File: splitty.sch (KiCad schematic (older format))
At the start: 97 parts, among them J1 USB_B_Micro, J2 USB_B_Micro, J3 Conn_01x06, J4 Conn_01x05, SW0 SW_Push, SW1 SW_Push, SW10 SW_Push, SW11 SW_Push, SW12 SW_Push, SW13 SW_Push, SW14 SW_Push, SW16 SW_Push, SW17 SW_Push, SW18 SW_Push, SW19 SW_Push, SW2 SW_Push, SW20 SW_Push, SW21 SW_Push, SW24 SW_Push, SW25 SW_Push, SW26 SW_Push, SW27 SW_Push, SW28 SW_Push, SW29 SW_Push, SW3 SW_Push, SW30 SW_Push, SW34 SW_Push, SW35 SW_Push, SW36 SW_Push, SW37 SW_Push, SW38 SW_Push, SW4 SW_Push, SW40 SW_Push, SW5 SW_Push, SW6 SW_Push, SW8 SW_Push, SW9 SW_Push, U1 ATmega32U4-AU, U2 USBLC6-2, U3 USBLC6-2, Y1 16M

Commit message: Update to Kicad 5
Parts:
- C1, C10, C11, C12, C3, C4, C5, C6, C7, C8, C9: footprint Capacitor_SMD:C_0603_1608Metric_Pad0.84x1.00mm_HandSolder -> Capacitor_SMD:C_0603_1608Metric_Pad1.05x0.95mm_HandSolder; symbol C -> Device:C
- D0, D1, D10, D11, D12, D13, D14, D16, D17, D18, D19, D2, D20, D21, D24, D25, D26, D27, D28, D29, D3, D30, D34, D35, D36, D37, D38, D4, D5, D6, D8, D9: symbol D -> Device:D
- J1, J2: symbol USB_B_Micro -> Connector:USB_B_Micro
- J3: symbol Conn_01x06 -> Connector_Generic:Conn_01x06
- J4: symbol Conn_01x05 -> Connector_Generic:Conn_01x05
- MK1, MK2, MK3, MK4, MK5, MK6, MK7, MK8: symbol Mounting_Hole -> Mechanical:MountingHole
- R1, R2, R3, R4, R5: footprint Resistor_SMD:R_0603_1608Metric_Pad0.84x1.00mm_HandSolder -> Resistor_SMD:R_0603_1608Metric_Pad1.05x0.95mm_HandSolder; symbol R -> Device:R
- SW0, SW1, SW10, SW11, SW12, SW13, SW14, SW16, SW17, SW18, SW19, SW2, SW20, SW21, SW24, SW25, SW26, SW27, SW28, SW29, SW3, SW30, SW34, SW35, SW36, SW37, SW38, SW4, SW40, SW5, SW6, SW8, SW9: symbol SW_Push -> Switch:SW_Push
- U1: symbol ATmega32U4-AU -> MCU_Microchip_ATmega:ATmega32U4-AU
- U2, U3: symbol USBLC6-2 -> splitty:USBLC6-2
- Y1: symbol Crystal -> Device:Crystal
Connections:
- wire segments 151 -> 219
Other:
- moved on the sheet: C1, C3, C4, C5, R3, SW40, Y1

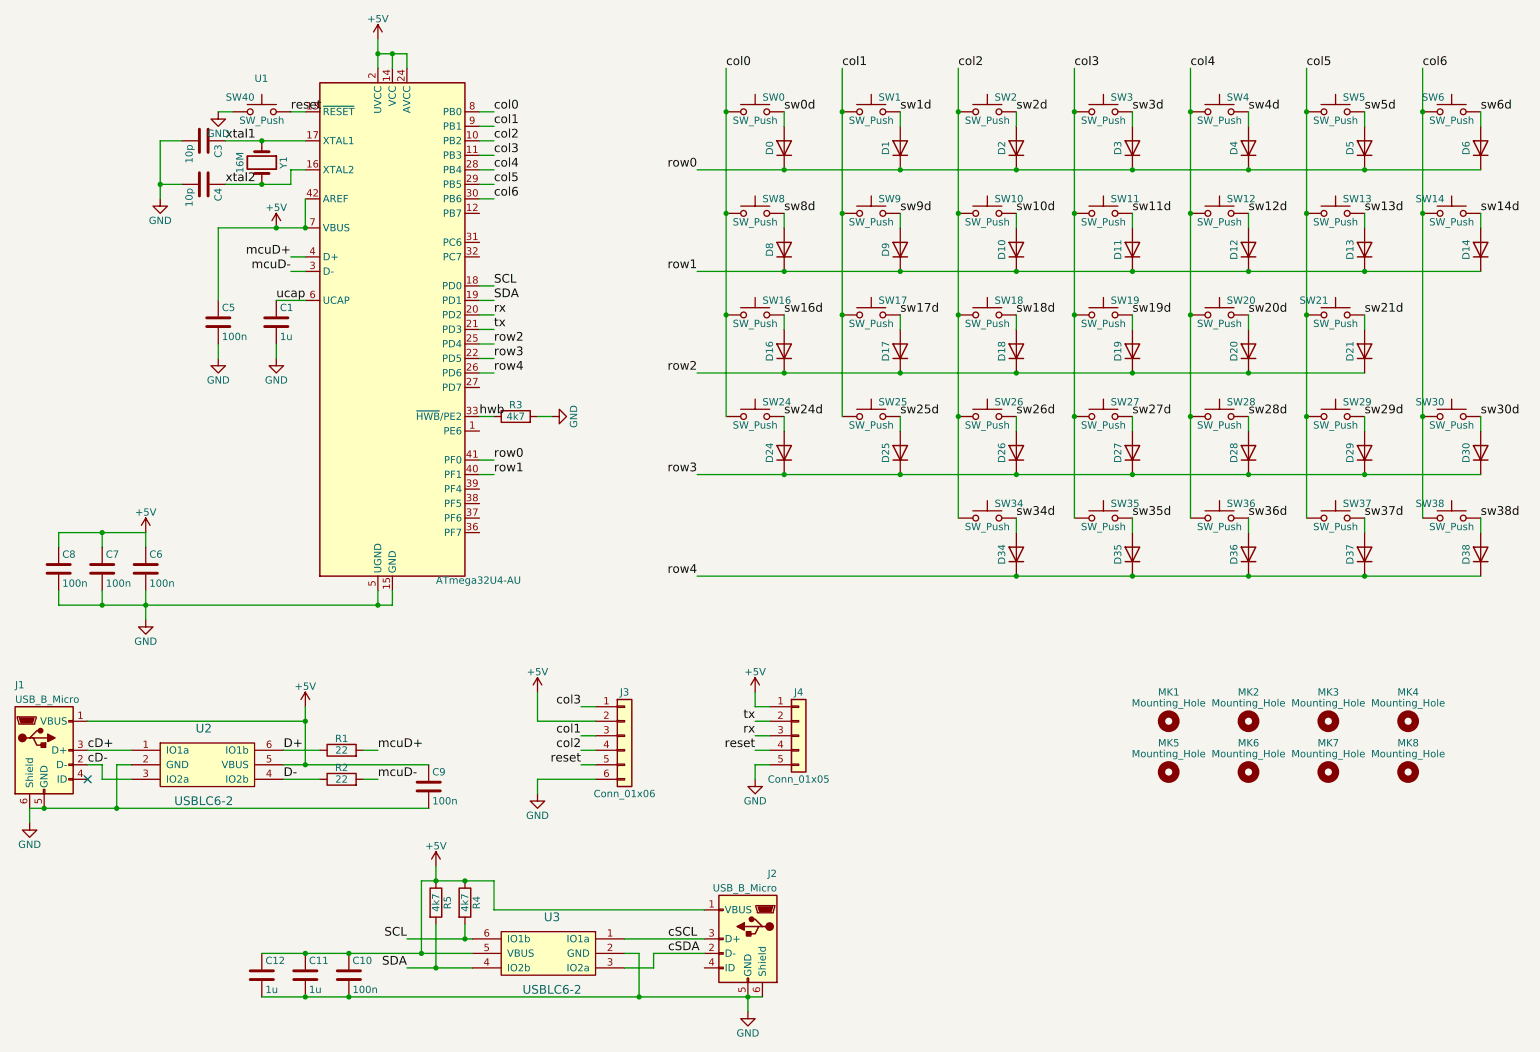
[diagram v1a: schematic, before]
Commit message: Add more copyright and license info, upgrade Kicad
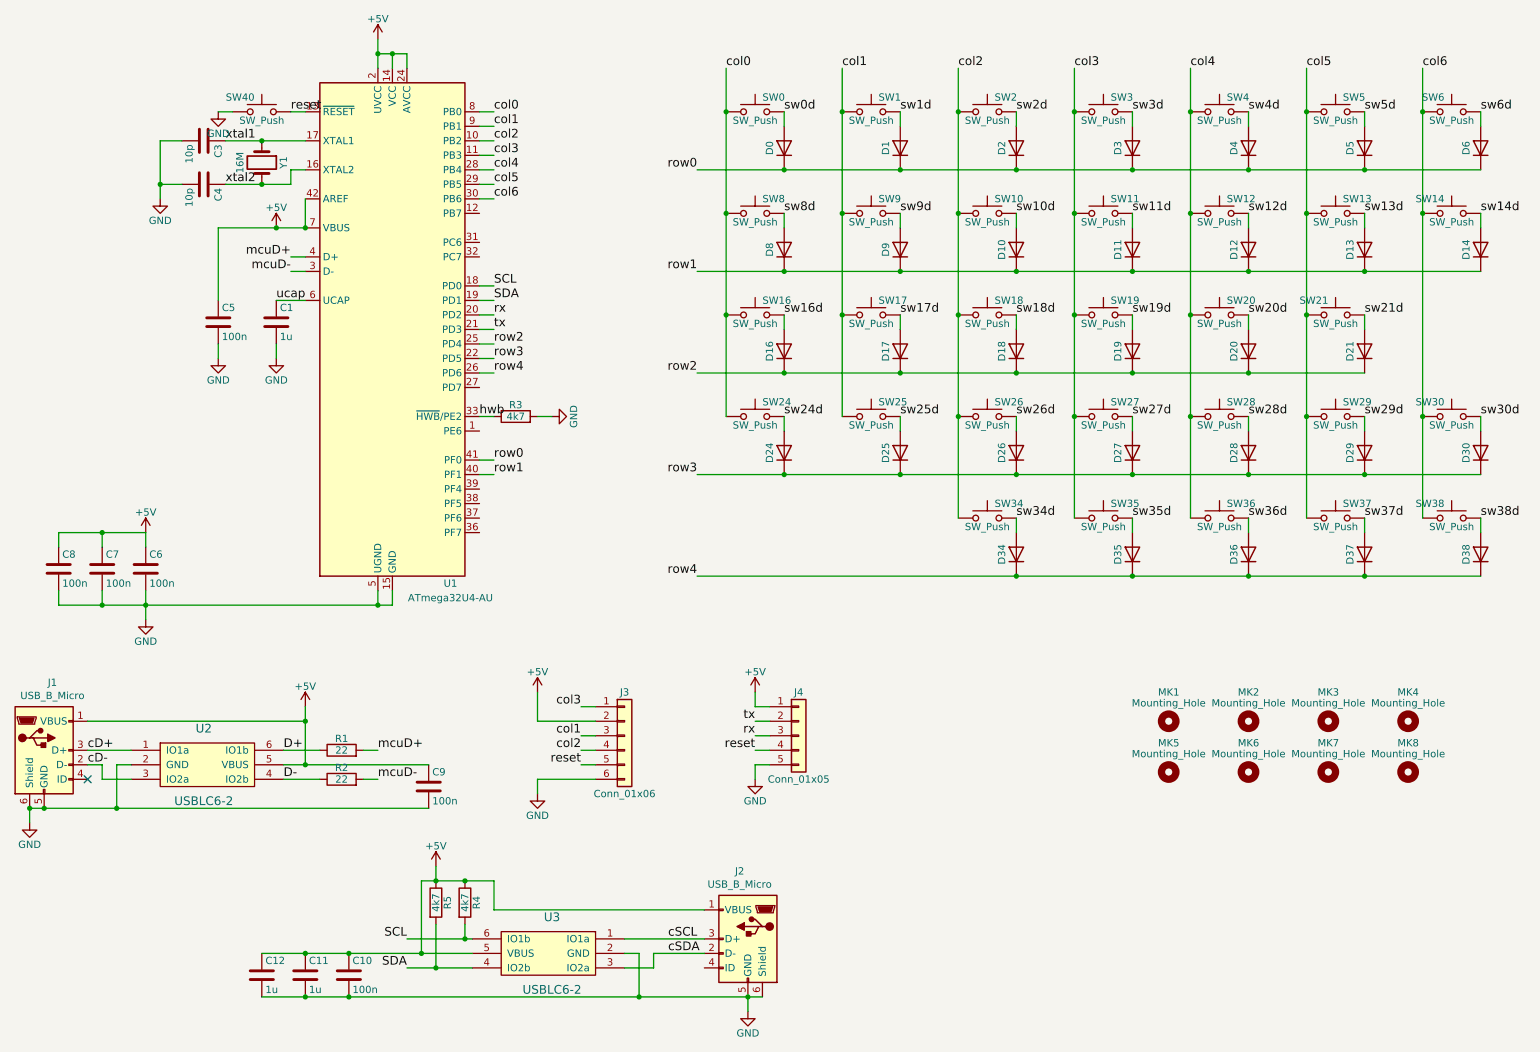
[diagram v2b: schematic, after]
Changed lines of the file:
@@
 EESchema Schematic File Version 4
-LIBS:splitty-cache
-EELAYER 26 0
+EELAYER 30 0
 EELAYER END
 $Descr A4 11693 8268
 encoding utf-8
 Sheet 1 1
-Title ""
-Date ""
-Rev ""
+Title "Splitty ergonomic keyboard"
+Date "2018-05-01"
+Rev "1"
 Comp ""
 Comment1 ""
 Comment2 ""
-Comment3 ""
-Comment4 ""
+Comment3 "License: MIT"
+Comment4 "Copyright © 2018 Nicolas Schodet"
 $EndDescr
-$Comp
-L MCU_Microchip_ATmega:ATmega32U4-AU U1
-U 1 1 5AD20652
-P 3400 2800
-F 0 "U1" H 2450 4500 50  0000 L BNN
-F 1 "ATmega32U4-AU" H 3700 1100 50  0000 L TNN
-F 2 "Package_QFP:TQFP-44_10x10mm_P0.8mm" H 3400 2800 50  0001 C CIN
-F 3 "" H 3400 2800 50  0001 C CNN
-	1    3400 2800
-	1    0    0    -1
-$EndComp
 $Comp
 L Switch:SW_Push SW0
@@
 Wire Wire Line
 	1700 4600 1700 4700
-$Comp
-L Connector:USB_B_Micro J1
-U 1 1 5AE7A997
-P 1000 5700
-F 0 "J1" H 800 6150 50  0000 L CNN
-F 1 "USB_B_Micro" H 800 6050 50  0000 L CNN
-F 2 "splitty:USB_Micro-B_Wuerth_629105150521_BothSides" H 1150 5650 50  0001 C CNN
-F 3 "" H 1150 5650 50  0001 C CNN
-	1    1000 5700
-	1    0    0    -1
-$EndComp
 Wire Wire Line
 	2800 1300 2700 1300
@@
 Wire Wire Line
 	2800 2400 2700 2400
-Wire Wire Line
-	1600 5700 1300 5700
 NoConn ~ 1300 5900
 Wire Wire Line
 	900  6200 900  6100
-Wire Wire Line
-	900  6100 1000 6100
 $Comp
 L Device:C C3
@@
 $EndComp
 Wire Wire Line
-	1300 5800 1400 5800
-Wire Wire Line
 	1400 5800 1400 5900
 Wire Wire Line
@@
 Wire Wire Line
 	2650 5800 2800 5800
-Connection ~ 1000 6100
 $Comp
 L Device:C C9
@@
 	2800 5400 2800 5500
 Connection ~ 2800 5800
-Wire Wire Line
-	2800 5500 1300 5500
 Connection ~ 2800 5500
 Wire Wire Line
@@
 Text Label 10500 1000 0    60   ~ 0
 col6
-$Comp
-L Connector:USB_B_Micro J2
-U 1 1 5AF9B5B9
-P 5850 7000
-F 0 "J2" H 5650 7450 50  0000 L CNN
-F 1 "USB_B_Micro" H 5650 7350 50  0000 L CNN
-F 2 "splitty:USB_Micro-B_Wuerth_629105150521_BothSides" H 6000 6950 50  0001 C CNN
-F 3 "" H 6000 6950 50  0001 C CNN
-	1    5850 7000
-	-1   0    0    -1
-$EndComp
 Wire Wire Line
 	3600 6600 3600 7100
@@
 	1400 4200 1700 4200
 Wire Wire Line
-	1000 6100 1500 6100
-Wire Wire Line
 	5850 7400 5950 7400
 Wire Wire Line
@@
 Wire Wire Line
 	2800 1900 2800 2100
-Connection ~ 2800 2100
 Connection ~ 2600 2100
 Wire Wire Line
@@
 Wire Wire Line
 	10500 1300 10500 2000
+Wire Wire Line
+	1600 5700 1300 5700
+Wire Wire Line
+	1300 5800 1400 5800
+Wire Wire Line
+	2800 5500 1300 5500
+$Comp
+L Connector:USB_B_Micro J1
+U 1 1 60232DE7
+P 1000 5700
+F 0 "J1" H 1057 6167 50  0000 C CNN
+F 1 "USB_B_Micro" H 1057 6076 50  0000 C CNN
+F 2 "splitty:USB_Micro-B_Wuerth_629105150521_BothSides" H 1150 5650 50  0001 C CNN
+F 3 "~" H 1150 5650 50  0001 C CNN
+	1    1000 5700
+	1    0    0    -1
+$EndComp
+Wire Wire Line
+	900  6100 1000 6100
+Connection ~ 900  6100
+Wire Wire Line
+	1500 6100 1000 6100
+Connection ~ 1000 6100
+$Comp
+L Connector:USB_B_Micro J2
+U 1 1 60283DA3
+P 5850 7000
+F 0 "J2" H 5907 7467 50  0000 C CNN
+F 1 "USB_B_Micro" H 5907 7376 50  0000 C CNN
+F 2 "splitty:USB_Micro-B_Wuerth_629105150521_BothSides" H 6000 6950 50  0001 C CNN
+F 3 "~" H 6000 6950 50  0001 C CNN
+	1    5850 7000
+	-1   0    0    -1
+$EndComp
+$Comp
+L MCU_Microchip_ATmega:ATmega32U4-AU U1
+U 1 1 602BC75E
+P 3400 2800
+F 0 "U1" H 3800 1050 50  0000 C CNN
+F 1 "ATmega32U4-AU" H 3800 950 50  0000 C CNN
+F 2 "Package_QFP:TQFP-44_10x10mm_P0.8mm" H 3400 2800 50  0001 C CIN
+F 3 "http://ww1.microchip.com/downloads/en/DeviceDoc/Atmel-7766-8-bit-AVR-ATmega16U4-32U4_Datasheet.pdf" H 3400 2800 50  0001 C CNN
+	1    3400 2800
+	1    0    0    -1
+$EndComp
+Connection ~ 2800 2100
 $EndSCHEMATC
